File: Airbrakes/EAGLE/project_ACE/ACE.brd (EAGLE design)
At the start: 100 x 62 mm, 12 parts, among them J3 PTH

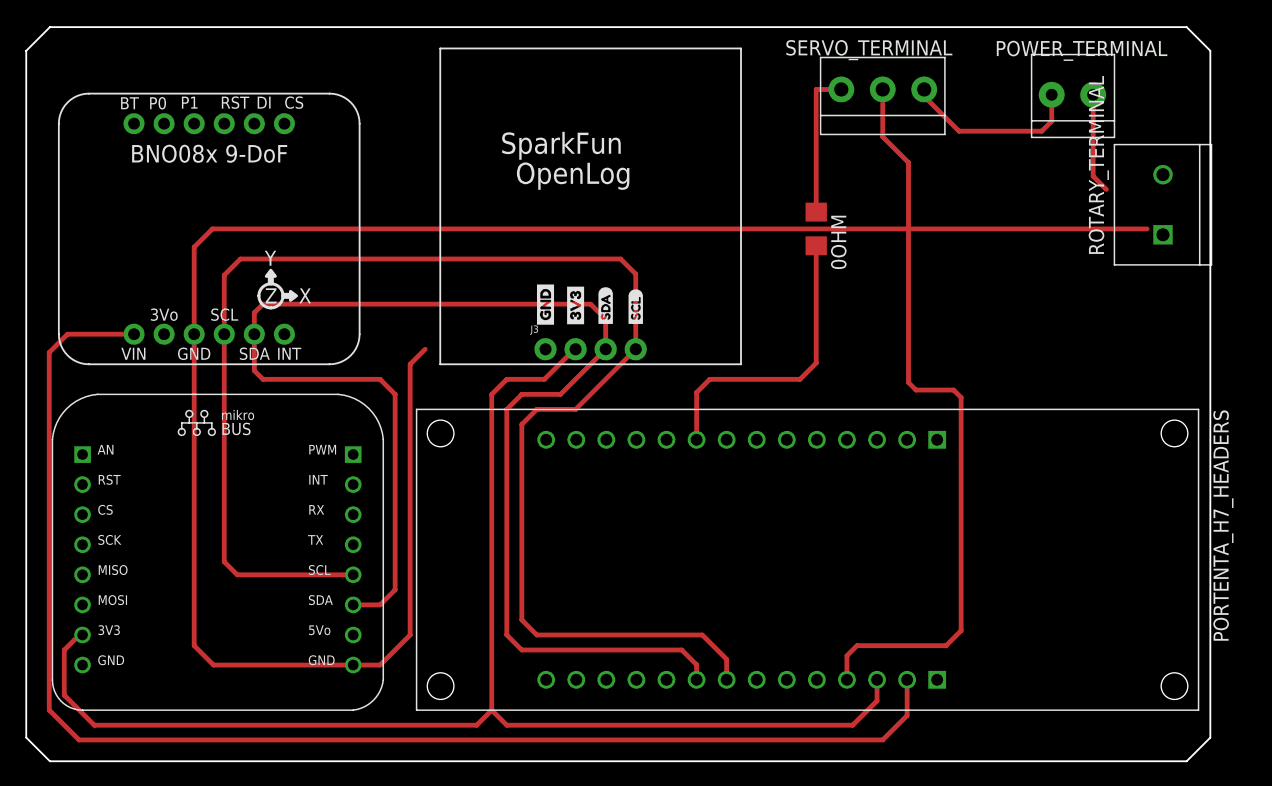
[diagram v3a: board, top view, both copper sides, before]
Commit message: Finalized Review of v0.1.0 SS ACE
* Changed all terminal block to 200mil pitch
* Rerouted servo power switching
* Verify traces and add GND copper pour
* Spruce up silkscreen
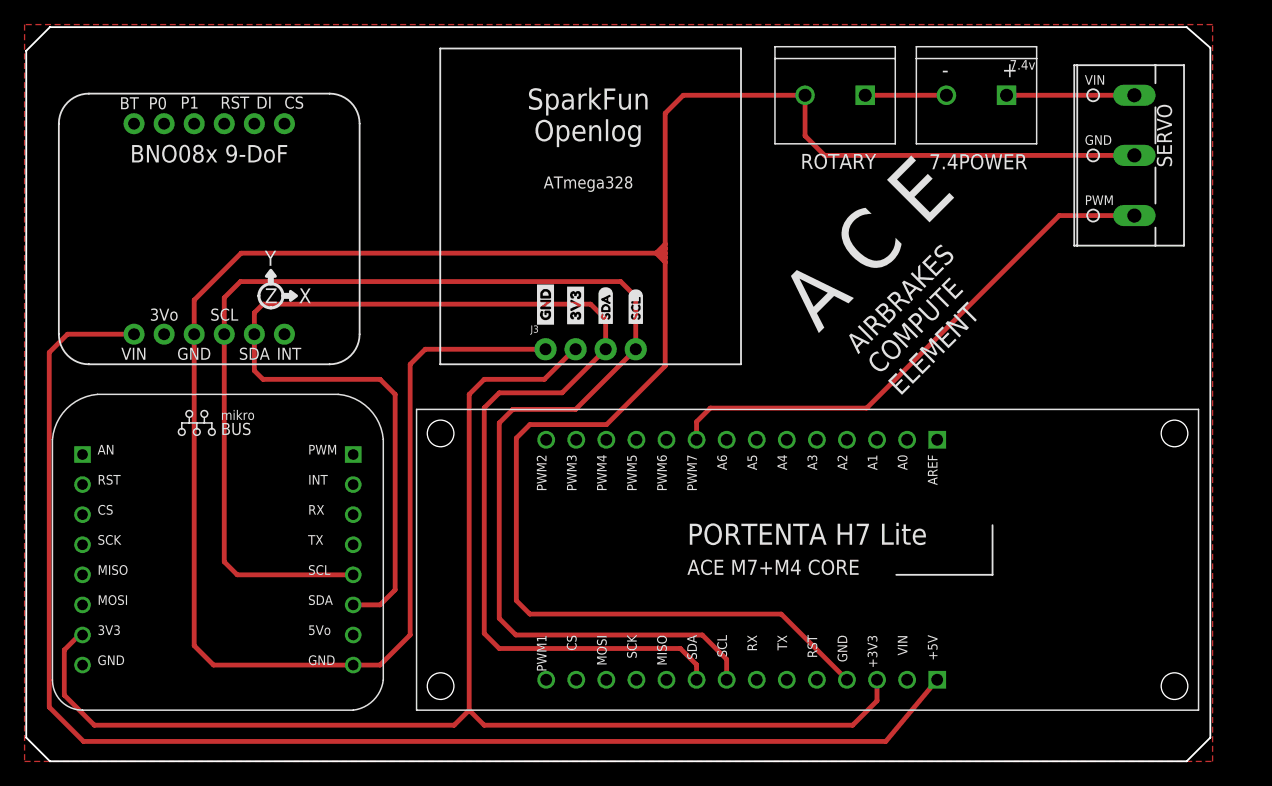
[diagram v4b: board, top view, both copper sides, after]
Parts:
- removed 0OHM: (no value), fab_new:R1206
- removed POWER_TERMINAL: CONN_02_TERM-ADAFRUIT, fab_new:3.5MMTERM
- removed SERVO_TERMINAL: CONN_03_TERM'-FABLAB', fab_new:ED555DS-3DS
- added 7.4POWER: 282837-2, 282837-2:TE_282837-2
- added SERVO: (no value), con-wago-508:W237-3E
- moved ROTARY_TERMINAL 29.2 mm to (91.3, 63.2), turned to 180 degrees
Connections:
- removed net 7.4V: POWER_TERMINAL.2, SERVO_TERMINAL.3
- removed net N$2: J3.1, ROTARY_TERMINAL.1, ROTARY_TERMINAL.2
- removed net PWM: 0OHM.1, 0OHM.2, SERVO_TERMINAL.1, U$10.J9
- new net SERVO_GND: 7.4POWER.2, ROTARY_TERMINAL.1
- new net SERVO_PWM: SERVO.1, U$10.J9
- new net SERVO_VIN: 7.4POWER.1, SERVO.3
- net GND: now also J3.1, ROTARY_TERMINAL.2, SERVO.2; no longer POWER_TERMINAL.1, SERVO_TERMINAL.2
- net VCC: now also U$10.J15; no longer U$10.J16
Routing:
- net SERVO_PWM: track 0.00 -> 45.7 mm
- net PWM: track 37.5 -> 0.00 mm
- net GND: track 230.7 -> 253.8 mm
- net 7.4V: track 15.2 -> 0.00 mm
- net SERVO_VIN: track 0.00 -> 10.8 mm
- net SERVO_GND: track 0.00 -> 6.86 mm
- net SDA: track 119.1 -> 122.9 mm
- net 3.3V: track 114.6 -> 116.5 mm
- net VCC: track 115.4 -> 116.4 mm
- added copper zone on layer 1, net GND
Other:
- outline, holes or cut-outs redrawn
- board text added: "+"
- board text added: "-"
- board text added: "7.4v"
- board text added: "A C E"
- board text added: "AIRBRAKES COMPUTE ELEMENT"
- board text added: "ATmega328"
- board text added: "GND"
- board text added: "PWM"
- board text added: "ROTARY"
- board text added: "SparkFun Openlog"
- board text added: "VIN"
- board text removed: "OpenLog"
- board text removed: "SERVO_TERMINAL"
- board text removed: "SparkFun"

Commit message: Add ACE PCB v0.2.0
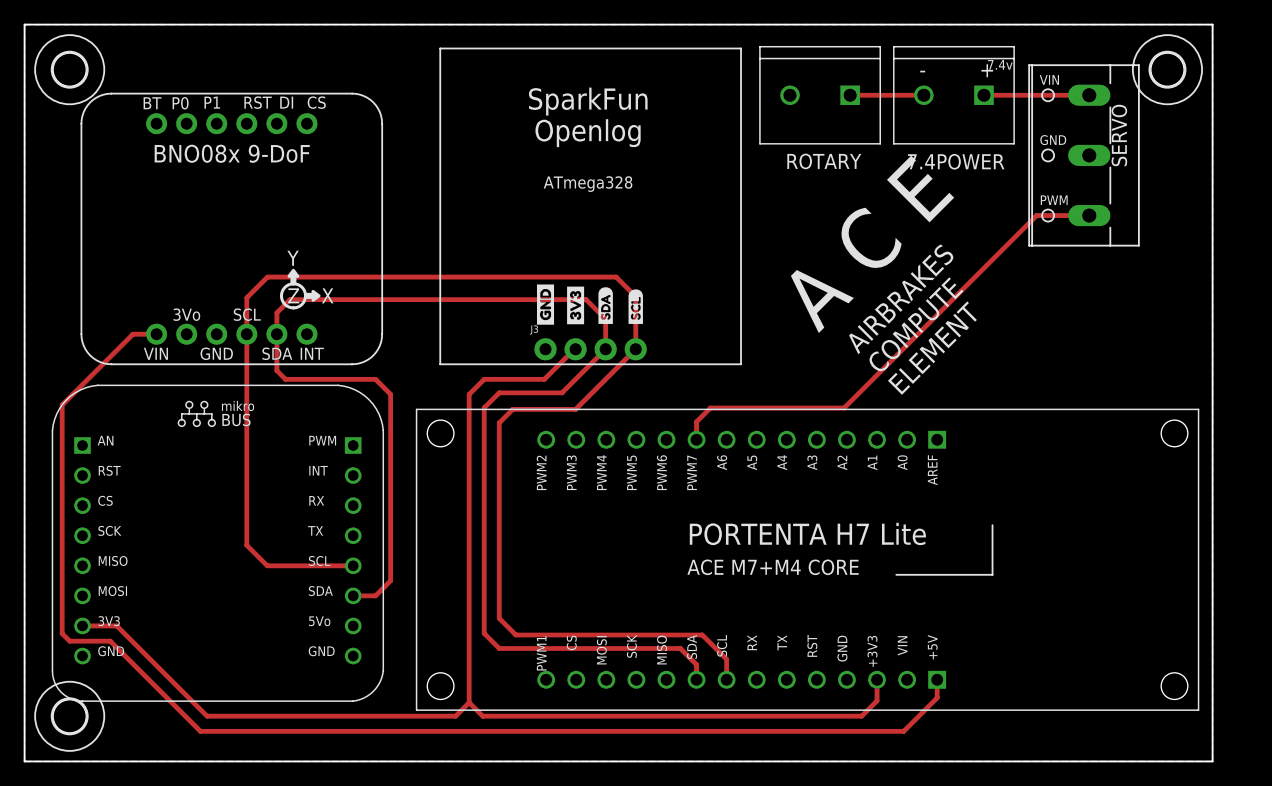
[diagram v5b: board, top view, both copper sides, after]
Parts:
- added U$13, U$14, U$15: (no value), holes:2,8
- moved SERVO 3.81 mm to (112.1, 58.2)
- moved 7.4POWER 1.91 mm to (101.3, 63.2)
- moved U$5 1.90 mm to (26.4, 39.3)
- moved ROTARY_TERMINAL 1.27 mm to (90.0, 63.2)
- moved U$1 0.76 mm to (25.2, 10.8)
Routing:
- net GND: track 253.8 -> 0.00 mm
- net VCC: track 116.4 -> 109.8 mm
- net 3.3V: track 116.5 -> 110.1 mm
- net SDA: track 122.9 -> 117.9 mm
- net SCL: track 126.9 -> 122.3 mm
- net SERVO_PWM: track 45.7 -> 41.9 mm
- net SERVO_VIN: track 10.8 -> 8.89 mm
- net SERVO_GND: track 6.86 -> 6.22 mm
- added copper zone on layer 16, net GND
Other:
- board size 100 x 62 mm -> 100.3 x 62.2 mm
- board text added: "@WURocketry - Airbrakes 2023"
- board text added: "now with PADS! (on the bottom...)"
